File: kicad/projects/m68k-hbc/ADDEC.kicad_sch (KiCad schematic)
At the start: 20 parts, among them J1 JTAG_ADDEC, U10 EPM7128SLC84 / Address Decoder, U11 74LS137, U41 74LS139, U9 74LS137, X5 70M

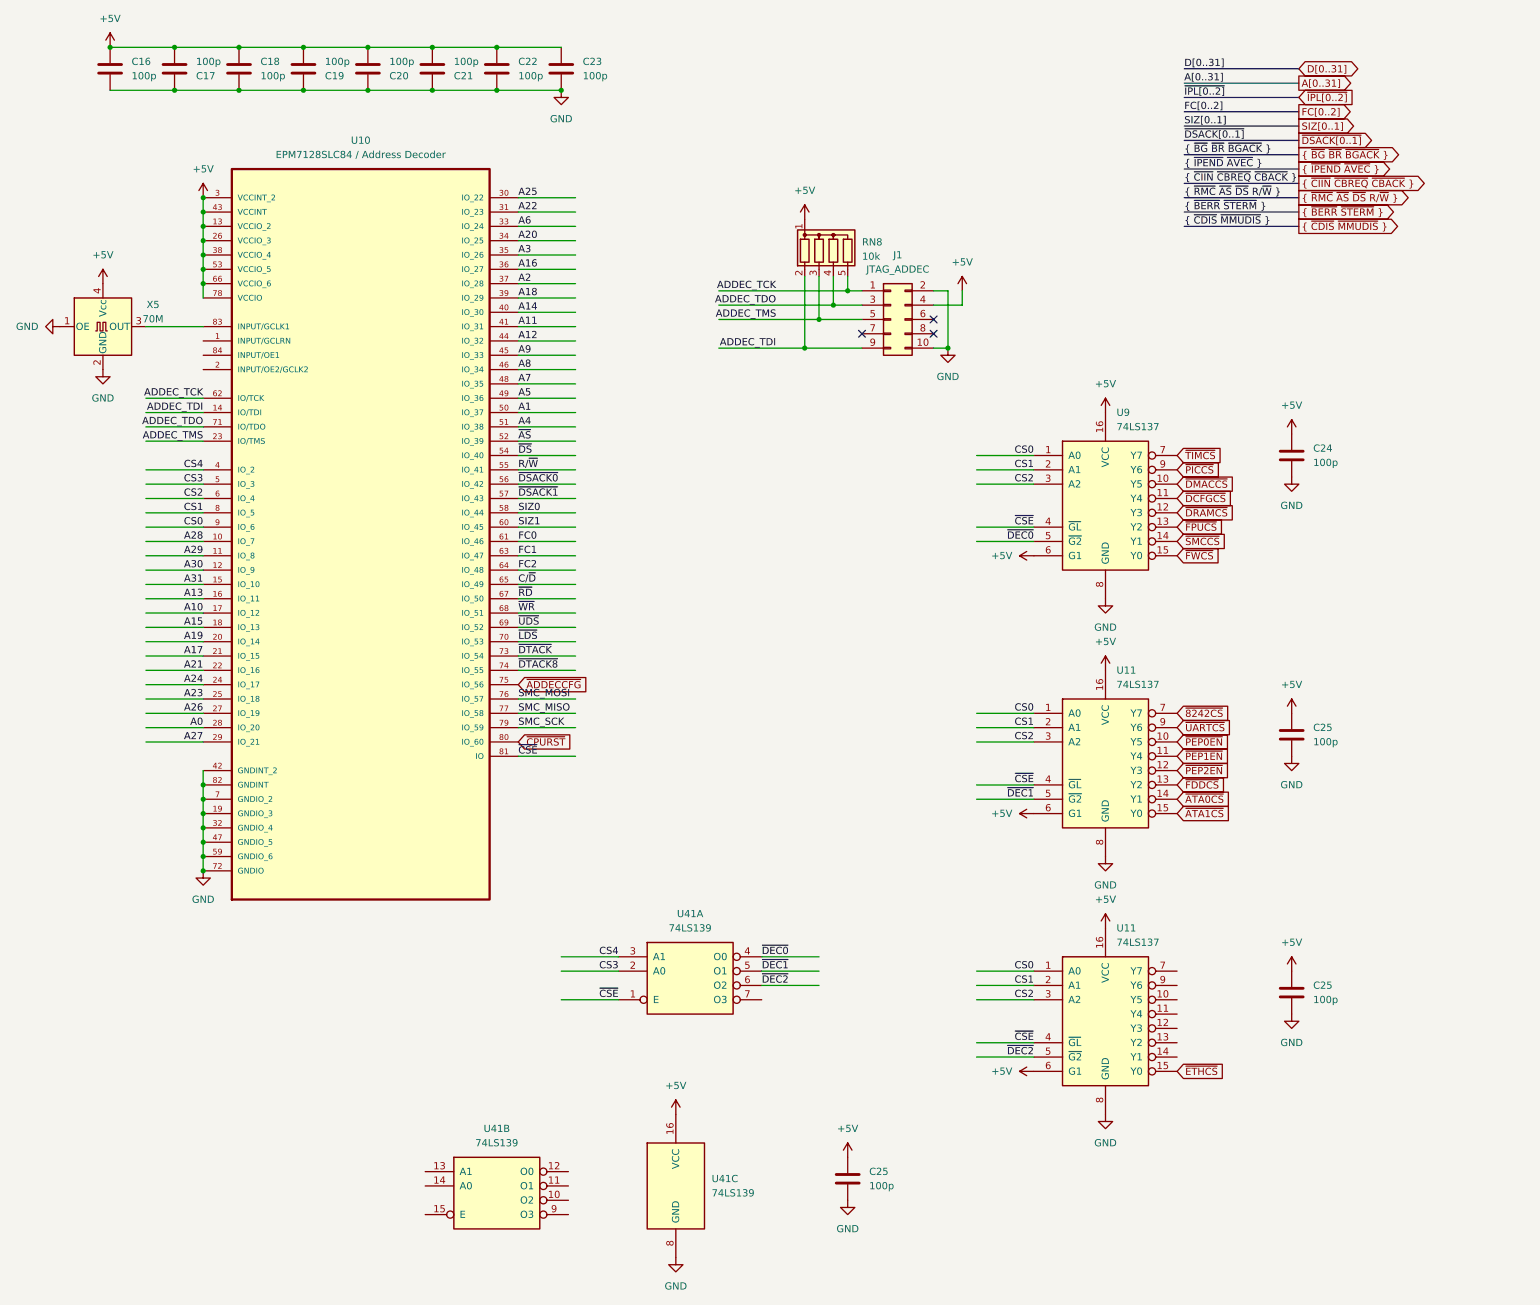
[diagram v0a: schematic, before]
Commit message: Modified system architecture, New KiCad Project: Cache Memory Module(SIMM80)
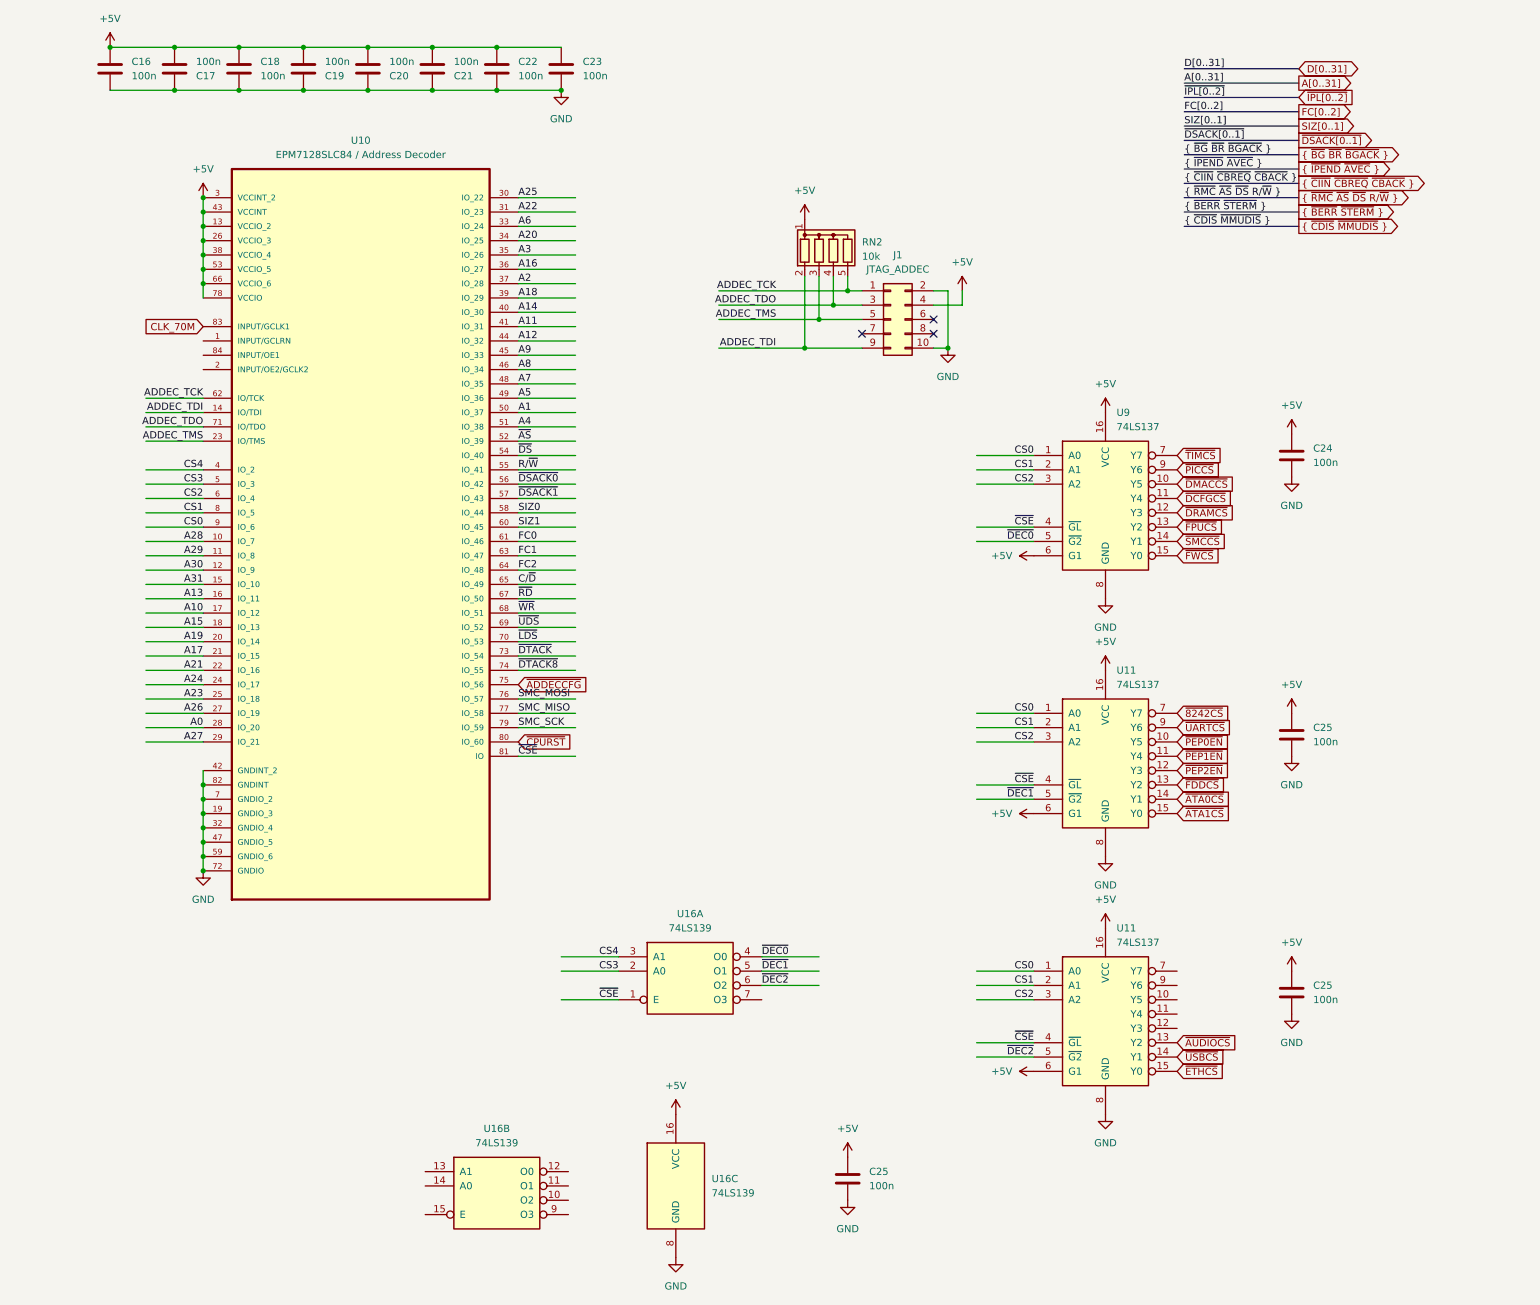
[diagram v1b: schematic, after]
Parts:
- removed X5: 70M, Oscillator:Oscillator_SMD_SeikoEpson_SG8002CA-4Pin_7.0x5.0mm, symbol Oscillator:SG-8002CA
- C16, C17, C18, C19, C20, C21, C22, C23, C24, C25: value 100p -> 100n
- renumbered RN8 to RN2, U41 to U16
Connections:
- net ~{AUDIOCS}: now reaches U11.13 (Y2)
- net ~{USBCS}: now reaches U11.14 (Y1)
- net CLK_70M: now reaches U10.83 (INPUT/GCLK1)

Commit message: Some Updates
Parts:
- removed C25: 100n, Capacitor_SMD:C_1206_3216Metric_Pad1.33x1.80mm_HandSolder, symbol Device:C
- removed U16: 74LS139, Package_SO:SOIC-16W_5.3x10.2mm_P1.27mm, symbol 74xx:74LS139
